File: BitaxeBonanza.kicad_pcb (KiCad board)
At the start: 6 copper layers, 65 x 112 mm, 174 parts, among them J1 XT30, J3 Conn_01x04, J4 USB_C_Receptacle_USB2.0, J5 Conn_01x06, J7 Conn_01x04, J8 TC2030-IDC, SW1 SWITCH-SPST, SW2 SWITCH-SPST, U1 TPS546D24ARVFR, U10 25MHz, U11 Treasure L2R, U12 Treasure R2L, U13 EMC2103-2, U14 SN74AVC4T774, U15 ISO6520, U2 TLV75515PDQNR, U3 TPSM861253RDXR, U4 TPS546D24ARVFR, U5 L78L05_SOT89, U6 ESP32-S3-WROOM-1, U7 TLV755075PDQNR, U8 TLV75515PDQNR, U9 TLV755075PDQNR

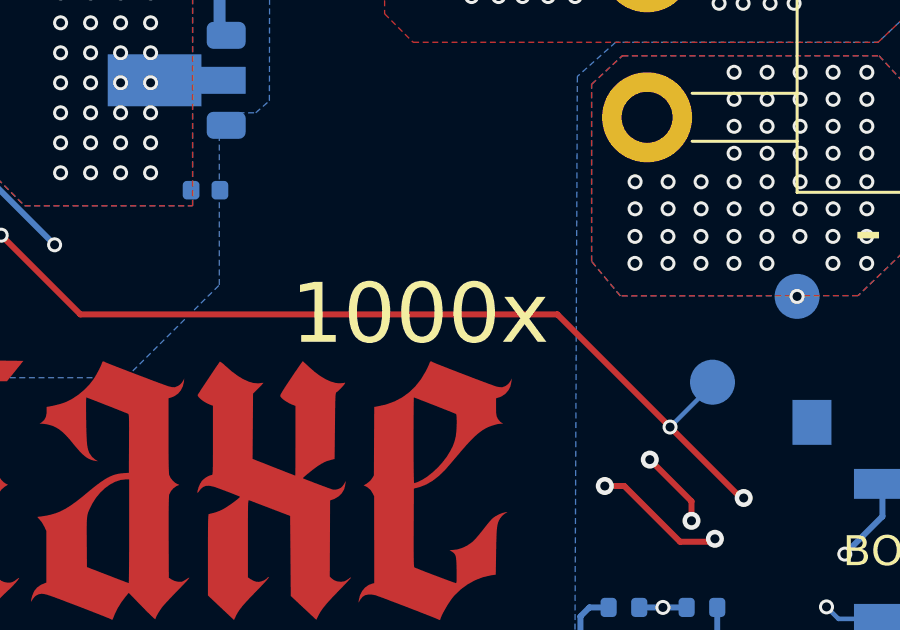
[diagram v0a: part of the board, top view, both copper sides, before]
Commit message: added 8 ASICs in schematic
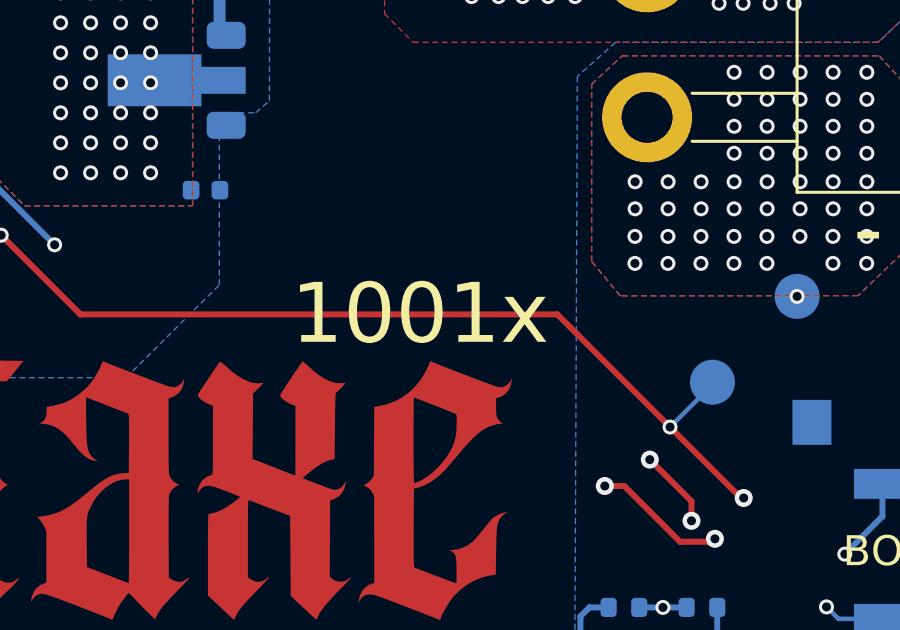
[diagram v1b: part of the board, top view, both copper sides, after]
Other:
- board text added: "1001x"
- board text removed: "1000x"
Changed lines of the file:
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@@
 		)
 	)
-	(gr_text "1000x"
+	(gr_text "1001x"
 		(at 138.48 67.98 0)
 		(layer "F.SilkS")

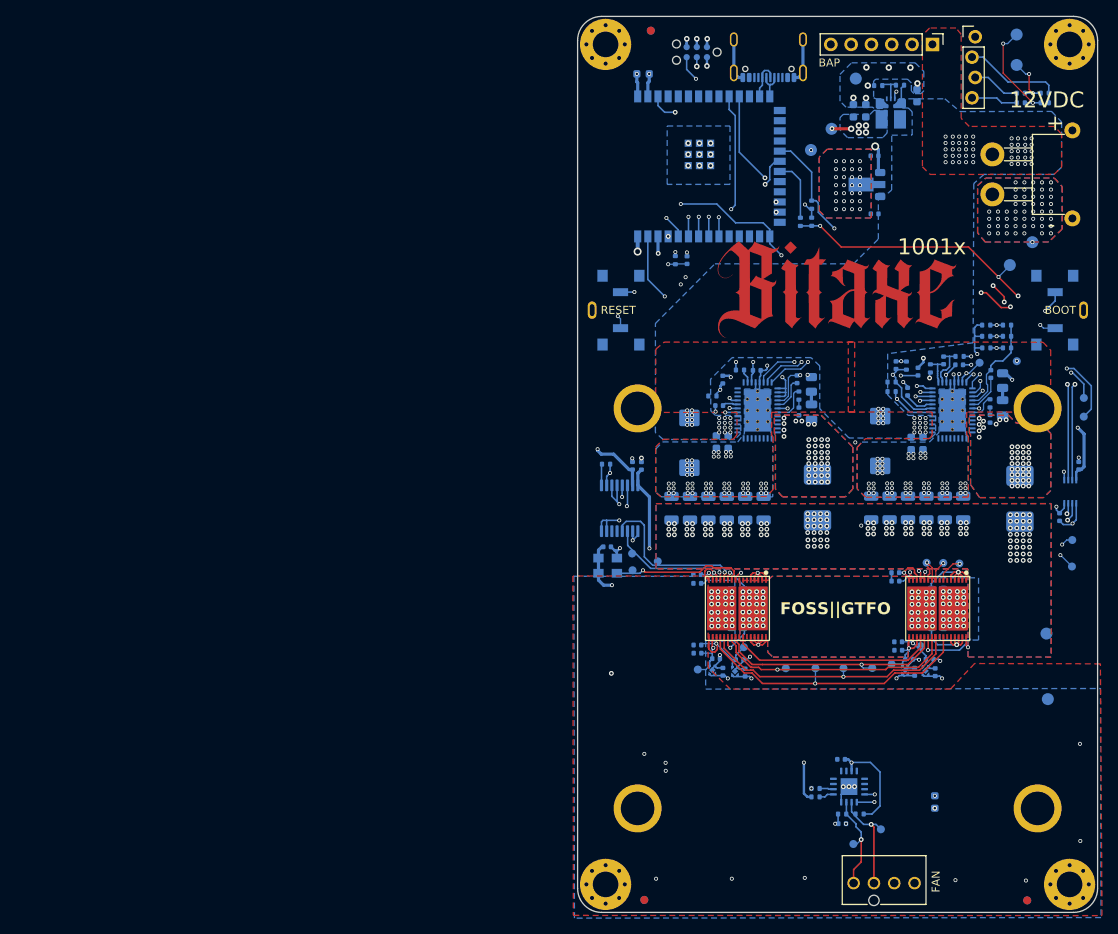
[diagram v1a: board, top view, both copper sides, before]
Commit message: moved ASIC bypass caps out to separate sheet
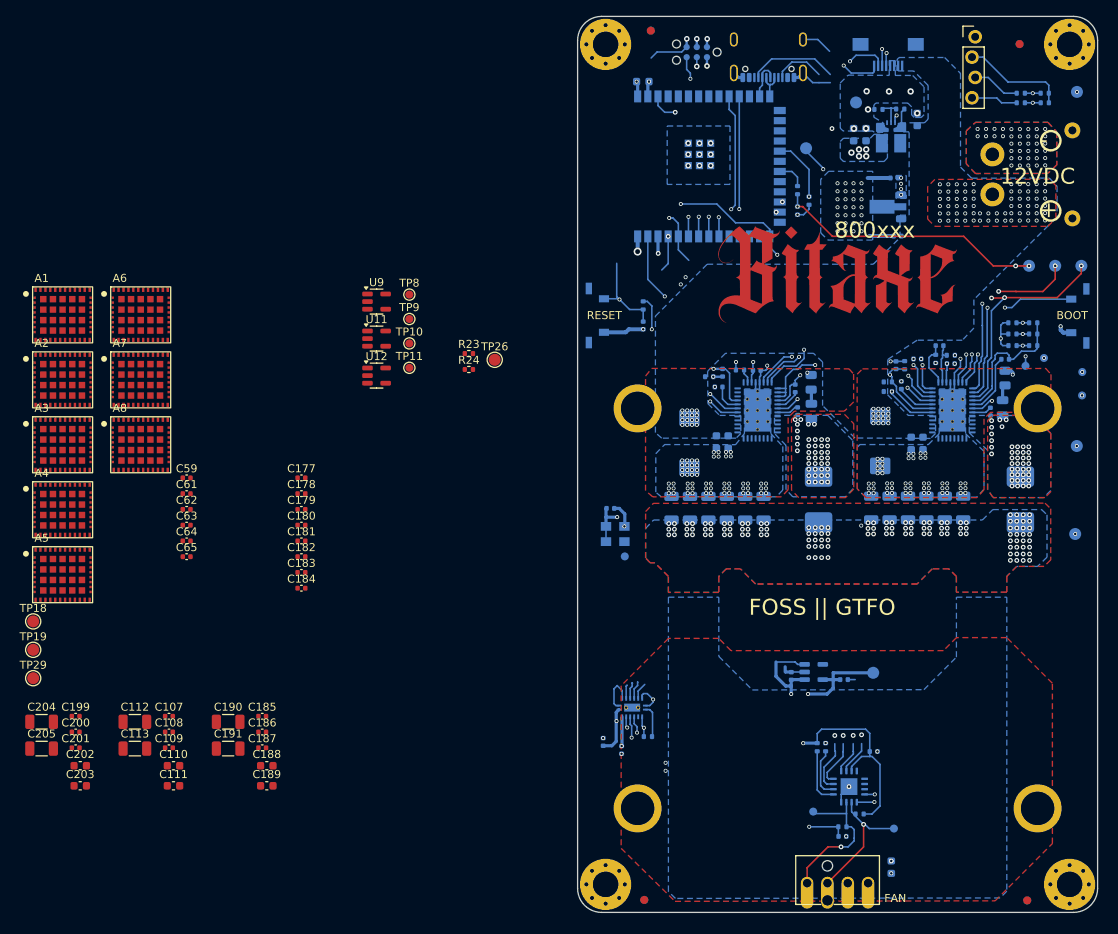
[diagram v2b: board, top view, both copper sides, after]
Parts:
- removed the C21 at (119.4, 120.0)
- removed the C38 at (116.7, 119.9)
- removed C40, C50, C51, C52, C53, C54, C57, C58: 1uF, Capacitor_SMD:C_0402_1005Metric
- removed C66, C67, C68, C69, C73, C74, C75, C76: 10uF, Capacitor_SMD:C_0603_1608Metric
- removed C70, C71: 0.1uF, Capacitor_SMD:C_0402_1005Metric
- removed FID5, FID6: Fiducial_back, Fiducial:Fiducial_1mm_Mask2mm
- removed H16: Heatsink Mounts, bitaxe:GT_heatsink
- removed J5: Conn_01x06, Connector_PinHeader_2.54mm:PinHeader_1x06_P2.54mm_Vertical
- removed TP12, TP13, TP14: ~, TestPoint:TestPoint_Pad_D1.0mm
- removed TP2: 1V5, TestPoint:TestPoint_Pad_D1.0mm
- removed TP4: 0V75, TestPoint:TestPoint_Pad_D1.0mm
- removed TP5: 1V5-0, TestPoint:TestPoint_Pad_D1.0mm
- removed TP6: 0V75-0, TestPoint:TestPoint_Pad_D1.0mm
- removed U14: SN74AVC4T774, Package_SO:TSSOP-16_4.4x5mm_P0.65mm
- removed U15: ISO6520, bitaxe:ISO6520FREUR
- removed U8: TLV75515PDQNR, bitaxe:DQN0004A
- added A1: BZM2_MODE1, bitaxe:bzm2, F.Cu at (34.1, 75.3)
- added A2: BZM2_MODE1, bitaxe:bzm2, F.Cu at (34.1, 83.4)
- added A3: BZM2_MODE0, bitaxe:bzm2, F.Cu at (34.1, 91.5)
- added A4: BZM2_MODE0, bitaxe:bzm2, F.Cu at (34.1, 99.7)
- added A5: BZM2_MODE1, bitaxe:bzm2, F.Cu at (34.1, 107.8)
- added A6: BZM2_MODE1, bitaxe:bzm2, F.Cu at (43.9, 75.3)
- added A7: BZM2_MODE0, bitaxe:bzm2, F.Cu at (43.9, 83.4)
- added A8: BZM2_MODE0, bitaxe:bzm2, F.Cu at (43.9, 91.5)
- added C107: 0.1uF, Capacitor_SMD:C_0402_1005Metric, F.Cu at (47.4, 125.5)
- added C108: 0.1uF, Capacitor_SMD:C_0402_1005Metric, F.Cu at (47.4, 127.5)
- added C109: 0.1uF, Capacitor_SMD:C_0402_1005Metric, F.Cu at (47.4, 129.4)
- added C110: 10uF, Capacitor_SMD:C_0603_1608Metric, F.Cu at (48.0, 131.7)
- added C111: 10uF, Capacitor_SMD:C_0603_1608Metric, F.Cu at (48.0, 134.2)
- added C112: 100uF, Capacitor_SMD:C_1206_3216Metric, F.Cu at (43.2, 126.2)
- added C113: 100uF, Capacitor_SMD:C_1206_3216Metric, F.Cu at (43.2, 129.5)
- added C177: 120pF, Capacitor_SMD:C_0402_1005Metric, F.Cu at (64.0, 95.7)
- added C178: 120pF, Capacitor_SMD:C_0402_1005Metric, F.Cu at (64.0, 97.7)
- added C179: 120pF, Capacitor_SMD:C_0402_1005Metric, F.Cu at (64.0, 99.6)
- added C180: 120pF, Capacitor_SMD:C_0402_1005Metric, F.Cu at (64.0, 101.6)
- added C181: 120pF, Capacitor_SMD:C_0402_1005Metric, F.Cu at (64.0, 103.6)
- added C182: 120pF, Capacitor_SMD:C_0402_1005Metric, F.Cu at (64.0, 105.5)
- added C183: 120pF, Capacitor_SMD:C_0402_1005Metric, F.Cu at (64.0, 107.5)
- added C184: 120pF, Capacitor_SMD:C_0402_1005Metric, F.Cu at (64.0, 109.5)
- added C185: 0.1uF, Capacitor_SMD:C_0402_1005Metric, F.Cu at (59.1, 125.5)
- added C186: 0.1uF, Capacitor_SMD:C_0402_1005Metric, F.Cu at (59.1, 127.5)
- added C187: 0.1uF, Capacitor_SMD:C_0402_1005Metric, F.Cu at (59.1, 129.4)
- added C188: 10uF, Capacitor_SMD:C_0603_1608Metric, F.Cu at (59.6, 131.7)
- added C189: 10uF, Capacitor_SMD:C_0603_1608Metric, F.Cu at (59.6, 134.2)
- added C190: 100uF, Capacitor_SMD:C_1206_3216Metric, F.Cu at (54.8, 126.2)
- added C191: 100uF, Capacitor_SMD:C_1206_3216Metric, F.Cu at (54.8, 129.5)
- added C199: 0.1uF, Capacitor_SMD:C_0402_1005Metric, F.Cu at (35.8, 125.5)
- added C200: 0.1uF, Capacitor_SMD:C_0402_1005Metric, F.Cu at (35.8, 127.5)
- added C201: 0.1uF, Capacitor_SMD:C_0402_1005Metric, F.Cu at (35.8, 129.4)
- added C202: 10uF, Capacitor_SMD:C_0603_1608Metric, F.Cu at (36.3, 131.7)
- added C203: 10uF, Capacitor_SMD:C_0603_1608Metric, F.Cu at (36.3, 134.2)
- added C204: 100uF, Capacitor_SMD:C_1206_3216Metric, F.Cu at (31.5, 126.2)
- added C205: 100uF, Capacitor_SMD:C_1206_3216Metric, F.Cu at (31.5, 129.5)
- added C59: 1uF, Capacitor_SMD:C_0402_1005Metric, F.Cu at (49.6, 95.7)
- added C61: 1uF, Capacitor_SMD:C_0402_1005Metric, F.Cu at (49.6, 97.7)
- added H5: MountingHole_Pad, bitaxe:Sinhoo SMTSO3015CTJ_nopaste, B.Cu at (156.0, 87.0)
- added H6: MountingHole_Pad, bitaxe:Sinhoo SMTSO3015CTJ_nopaste, B.Cu at (106.0, 87.0)
- added H7: MountingHole_Pad, bitaxe:Sinhoo SMTSO3015CTJ_nopaste, B.Cu at (106.0, 137.0)
- added H8: MountingHole_Pad, bitaxe:Sinhoo SMTSO3015CTJ_nopaste, B.Cu at (156.0, 137.0)
- added J2: Conn_01x08, bitaxe:FPC-SMD_P0.50-8P_FGS-XJ-H2.0, B.Cu at (137.3, 42.8)
- C62, C63, C64, C65, R23, R24, TP26: moved to F.Cu
- FID1, FID2, FID3: value Fiducial_front -> Fiducial; footprint Fiducial:Fiducial_1mm_Mask2mm -> bitaxe:Fiducial_1mm_Mask2mm
- FID4: value Fiducial_back -> Fiducial; footprint Fiducial:Fiducial_1mm_Mask2mm -> bitaxe:Fiducial_1mm_Mask2mm; moved to F.Cu
- J1: moved to B.Cu
- SW1, SW2: footprint bitaxe:SW_TL3336AF160Q -> bitaxe:SW_TL3330AF130QG_EWI
- TP10, TP11, TP8, TP9: value ~ -> CLKI; moved to F.Cu
- TP16: value ~ -> 1V2; footprint TestPoint:TestPoint_Pad_D1.0mm -> TestPoint:TestPoint_Pad_D1.5mm
- TP18, TP19, TP29: value ~ -> 1V2; footprint TestPoint:TestPoint_Pad_D1.0mm -> TestPoint:TestPoint_Pad_D1.5mm; moved to F.Cu
- U11: value Treasure L2R -> MCP1824T-1202E/OT; footprint bitaxe:Auradine_Treasure -> Package_TO_SOT_SMD:SOT-23-5
- U12: value Treasure R2L -> MCP1824T-1202E/OT; footprint bitaxe:Auradine_Treasure -> Package_TO_SOT_SMD:SOT-23-5
- U2: value TLV75515PDQNR -> SN74AVC4T774; footprint bitaxe:DQN0004A -> bitaxe:BQB0016A-MFG
- U7: value TLV755075PDQNR -> MCP1824T-1202E/OT; footprint bitaxe:DQN0004A -> Package_TO_SOT_SMD:SOT-23-5
- U9: value TLV755075PDQNR -> MCP1824T-1202E/OT; footprint bitaxe:DQN0004A -> Package_TO_SOT_SMD:SOT-23-5; moved to F.Cu
- moved TP29 104.9 mm to (30.4, 120.7)
- moved TP19 101.3 mm to (30.4, 117.2)
- moved TP18 94.3 mm to (30.4, 113.6)
- moved C63 88.8 mm to (49.6, 101.6)
- moved C65 88.7 mm to (49.6, 105.5)
- moved TP11 86.5 mm to (77.5, 81.9)
- moved U9 82.7 mm to (73.4, 73.7), turned to 0 degrees
- moved TP8 76.5 mm to (77.5, 72.8)
- moved U12 75.9 mm to (73.4, 82.9), turned to 0 degrees
- moved TP9 73.4 mm to (77.5, 75.8)
- moved TP10 70.2 mm to (77.5, 78.9)
- moved R23 65.4 mm to (84.9, 80.1), turned to 0 degrees
- moved C62 64.5 mm to (49.6, 99.6)
- moved C64 64.0 mm to (49.6, 103.6)
- moved U11 56.3 mm to (73.4, 78.3), turned to 0 degrees
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- renumbered C48 to C21, C59 to C38, C61 to C48, R14 to R25
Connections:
- C38 pad 1: /ASIC/1V5 -> /ASIC/1V2
- C38 pad 2: GND -> /ASIC/GND
- C48 pad 2: GND -> /ASIC/GND
- C55 pad 1: GND -> /ASIC/GND
- C55 pad 2: /ASIC/0V75 -> /5V
- C56 pad 1: /ASIC/GND0 -> /ASIC/GND
- C56 pad 2: /ASIC/0V75-0 -> /ASIC/1V2
- C60 pad 2: GND -> /ASIC/GND
- C62 pad 1: GND -> /ASIC/GND2
- C62 pad 2: Net-(C62-Pad2) -> /5V
- C63 pad 1: /ASIC/GND0 -> /ASIC/GND2
- C63 pad 2: Net-(C63-Pad2) -> /ASIC/1V2-2
- C64 pad 1: GND -> /ASIC/GND3
- C64 pad 2: Net-(C64-Pad2) -> /5V
- C65 pad 1: /ASIC/GND0 -> /ASIC/GND3
- C65 pad 2: Net-(C65-Pad2) -> /ASIC/1V2-3
- R25 pad 1: GND -> /ASIC/GND
- R25 pad 2: Net-(U14-OE) -> Net-(U2-OE)
- TP10 pad 1: Net-(U12-CLOCK_O) -> Net-(A8-TX_IN)
- TP11 pad 1: /ASIC/RX_1V5 -> Net-(A8-TRIP_IN)
- TP16 pad 1: Net-(U11-RESET_N_O) -> /ASIC/1V2
- TP18 pad 1: Net-(U11-CLOCK_O) -> /ASIC/1V2-1
- TP19 pad 1: Net-(U11-COMMAND_O) -> /ASIC/1V2-2
- TP29 pad 1: Net-(U11-RESPONSE_O) -> /ASIC/1V2-3
- TP8 pad 1: Net-(U12-RESET_N_O) -> Net-(A8-RX_OUT)
- TP9 pad 1: Net-(U12-COMMAND_O) -> Net-(A8-RESET_OUT)
- U10 pad 2: GND -> /ASIC/GND
- U11 pad 1: GND -> /5V
- U11 pad 2: GND -> /ASIC/GND2
- U11 pad 3: GND -> /5V
- U11 pad 4: GND -> unconnected-(U11-PG-Pad4)
- U11 pad 5: GND -> /ASIC/1V2-2
- U12 pad 1: /ASIC/GND0 -> /5V
- U12 pad 2: /ASIC/GND0 -> /ASIC/GND3
- U12 pad 3: /ASIC/GND0 -> /5V
- U12 pad 4: /ASIC/GND0 -> unconnected-(U12-PG-Pad4)
- U12 pad 5: /ASIC/GND0 -> /ASIC/1V2-3
- U2 pad 1: /ASIC/1V5 -> /ASIC/GND
- U2 pad 2: GND -> /ASIC/GND
- U2 pad 3: /5V -> /ASIC/RST_1V2
- U2 pad 4: /5V -> /ASIC/TX_1V2
- U2 pad 5: GND -> /ASIC/RX_1V2
- U6 pad 20: /ASIC/TT_3V3 -> /ASIC/TRIP_3V3
- U7 pad 1: /ASIC/0V75 -> /5V
- U7 pad 2: GND -> /ASIC/GND
- U7 pad 4: /5V -> unconnected-(U7-PG-Pad4)
- U7 pad 5: GND -> /ASIC/1V2
- U9 pad 1: /ASIC/0V75-0 -> /5V
- U9 pad 2: /ASIC/GND0 -> /ASIC/GND1
- U9 pad 4: /5V -> unconnected-(U9-PG-Pad4)
- U9 pad 5: /ASIC/GND0 -> /ASIC/1V2-1
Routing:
- net (no net): track 0.00 -> 111.2 mm, vias 0 -> 4
- net /ASIC/1V2: track 0.00 -> 80.1 mm, vias 0 -> 4
- net /ASIC/TT_3V3: track 70.7 -> 0.00 mm, vias 2 -> 0
- net /3V3: track 213.7 -> 145.5 mm, vias 16 -> 13
- net /ASIC/GND0: track 65.9 -> 0.00 mm, vias 55 -> 0
- net /ASIC/1V5: track 61.5 -> 0.00 mm, vias 4 -> 0
- net /ASIC/1V5-0: track 44.0 -> 0.00 mm, vias 3 -> 0
- net Net-(U11-RESET_N_O): track 36.7 -> 0.00 mm, vias 1 -> 0
- net Net-(U11-COMMAND_O): track 33.8 -> 0.00 mm, vias 1 -> 0
- net /ASIC/TX_3V3: track 59.7 -> 93.5 mm
- net GND: track 81.8 -> 48.3 mm, vias 262 -> 216
- net Net-(U11-CLOCK_O): track 31.6 -> 0.00 mm, vias 1 -> 0
- net Net-(U11-RESPONSE_O): track 29.8 -> 0.00 mm, vias 1 -> 0
- net /ASIC/RX_1V5: track 29.1 -> 0.00 mm, vias 3 -> 0
- net /ASIC/TT_1V5: track 28.8 -> 0.00 mm, vias 3 -> 0
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- added copper zone on B.Cu, net /5V
- removed copper zone on B.Cu, net /ASIC/GND0
- removed copper zone on F.Cu, net /ASIC/GND0
- removed copper zone on In2.Cu, net /ASIC/GND0
- removed copper zone on In4.Cu, net /Power/SW2
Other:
- board text added: "800xxx"
- board text added: "FOSS || GTFO"
- board text removed: "1001x"
- board text removed: "FOSS||GTFO"

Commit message: made the board double wide. rough ASIC and vreg placement.
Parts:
- removed the TP16 at (135.4, 120.0)
- added C100: 10uF, Capacitor_SMD:C_0603_1608Metric, F.Cu at (38.0, 40.0)
- added C101: 100uF, Capacitor_SMD:C_1206_3216Metric, F.Cu at (33.1, 32.0)
- added C102: 100uF, Capacitor_SMD:C_1206_3216Metric, F.Cu at (33.1, 35.4)
- added C103: 0.1uF, Capacitor_SMD:C_0402_1005Metric, F.Cu at (72.4, 44.3)
- added C104: 0.1uF, Capacitor_SMD:C_0402_1005Metric, F.Cu at (72.4, 46.3)
- added C105: 0.1uF, Capacitor_SMD:C_0402_1005Metric, F.Cu at (72.4, 48.2)
- added C106: 10uF, Capacitor_SMD:C_0603_1608Metric, F.Cu at (73.0, 50.5)
- added C114: 10uF, Capacitor_SMD:C_0603_1608Metric, F.Cu at (61.3, 53.0)
- added C115: 100uF, Capacitor_SMD:C_1206_3216Metric, F.Cu at (56.5, 45.0)
- added C116: 100uF, Capacitor_SMD:C_1206_3216Metric, F.Cu at (56.5, 48.3)
- added C117: 0.1uF, Capacitor_SMD:C_0402_1005Metric, F.Cu at (37.4, 44.3)
- added C118: 0.1uF, Capacitor_SMD:C_0402_1005Metric, F.Cu at (37.4, 46.3)
- added C119: 0.1uF, Capacitor_SMD:C_0402_1005Metric, F.Cu at (37.4, 48.2)
- added C120: 10uF, Capacitor_SMD:C_0603_1608Metric, F.Cu at (38.0, 50.5)
- added C121: 10uF, Capacitor_SMD:C_0603_1608Metric, F.Cu at (38.0, 53.0)
- added C122: 100uF, Capacitor_SMD:C_1206_3216Metric, F.Cu at (33.1, 45.0)
- added C123: 100uF, Capacitor_SMD:C_1206_3216Metric, F.Cu at (33.1, 48.3)
- added C124: 0.1uF, Capacitor_SMD:C_0402_1005Metric, F.Cu at (60.7, 31.4)
- added C125: 0.1uF, Capacitor_SMD:C_0402_1005Metric, F.Cu at (60.7, 33.3)
- added C126: 0.1uF, Capacitor_SMD:C_0402_1005Metric, F.Cu at (60.7, 35.3)
- added C127: 10uF, Capacitor_SMD:C_0603_1608Metric, F.Cu at (61.3, 37.5)
- added C128: 10uF, Capacitor_SMD:C_0603_1608Metric, F.Cu at (61.3, 40.0)
- added C129: 100uF, Capacitor_SMD:C_1206_3216Metric, F.Cu at (56.5, 32.0)
- added C130: 100uF, Capacitor_SMD:C_1206_3216Metric, F.Cu at (56.5, 35.4)
- added C131: 0.1uF, Capacitor_SMD:C_0402_1005Metric, F.Cu at (72.4, 31.4)
- added C132: 0.1uF, Capacitor_SMD:C_0402_1005Metric, F.Cu at (72.4, 33.3)
- added C133: 0.1uF, Capacitor_SMD:C_0402_1005Metric, F.Cu at (72.4, 35.3)
- added C134: 10uF, Capacitor_SMD:C_0603_1608Metric, F.Cu at (73.0, 37.5)
- added C135: 10uF, Capacitor_SMD:C_0603_1608Metric, F.Cu at (73.0, 40.0)
- added C136: 100uF, Capacitor_SMD:C_1206_3216Metric, F.Cu at (68.1, 32.0)
- added C137: 100uF, Capacitor_SMD:C_1206_3216Metric, F.Cu at (68.1, 35.4)
- added C138: 0.1uF, Capacitor_SMD:C_0402_1005Metric, F.Cu at (49.1, 18.4)
- added C139: 0.1uF, Capacitor_SMD:C_0402_1005Metric, F.Cu at (49.1, 20.4)
- added C140: 0.1uF, Capacitor_SMD:C_0402_1005Metric, F.Cu at (49.1, 22.4)
- added C141: 10uF, Capacitor_SMD:C_0603_1608Metric, F.Cu at (49.6, 24.6)
- added C142: 10uF, Capacitor_SMD:C_0603_1608Metric, F.Cu at (49.6, 27.1)
- added C143: 100uF, Capacitor_SMD:C_1206_3216Metric, F.Cu at (44.8, 19.1)
- added C144: 100uF, Capacitor_SMD:C_1206_3216Metric, F.Cu at (44.8, 22.5)
- added C145: 0.1uF, Capacitor_SMD:C_0402_1005Metric, F.Cu at (60.7, 18.4)
- added C146: 0.1uF, Capacitor_SMD:C_0402_1005Metric, F.Cu at (60.7, 20.4)
- added C147: 0.1uF, Capacitor_SMD:C_0402_1005Metric, F.Cu at (60.7, 22.4)
- added C148: 10uF, Capacitor_SMD:C_0603_1608Metric, F.Cu at (61.3, 24.6)
- added C149: 10uF, Capacitor_SMD:C_0603_1608Metric, F.Cu at (61.3, 27.1)
- added C150: 100uF, Capacitor_SMD:C_1206_3216Metric, F.Cu at (56.5, 19.1)
- added C151: 100uF, Capacitor_SMD:C_1206_3216Metric, F.Cu at (56.5, 22.5)
- added C152: 0.1uF, Capacitor_SMD:C_0402_1005Metric, F.Cu at (49.1, 57.2)
- added C153: 0.1uF, Capacitor_SMD:C_0402_1005Metric, F.Cu at (49.1, 59.2)
- added C154: 0.1uF, Capacitor_SMD:C_0402_1005Metric, F.Cu at (49.1, 61.2)
- added C155: 10uF, Capacitor_SMD:C_0603_1608Metric, F.Cu at (49.6, 63.4)
- added C156: 10uF, Capacitor_SMD:C_0603_1608Metric, F.Cu at (49.6, 65.9)
- added C157: 100uF, Capacitor_SMD:C_1206_3216Metric, F.Cu at (44.8, 57.9)
- added C158: 100uF, Capacitor_SMD:C_1206_3216Metric, F.Cu at (44.8, 61.3)
- added C159: 0.1uF, Capacitor_SMD:C_0402_1005Metric, F.Cu at (72.4, 18.4)
- added C160: 0.1uF, Capacitor_SMD:C_0402_1005Metric, F.Cu at (72.4, 20.4)
- added C161: 0.1uF, Capacitor_SMD:C_0402_1005Metric, F.Cu at (72.4, 22.4)
- added C162: 10uF, Capacitor_SMD:C_0603_1608Metric, F.Cu at (73.0, 24.6)
- added C163: 10uF, Capacitor_SMD:C_0603_1608Metric, F.Cu at (73.0, 27.1)
- added C164: 100uF, Capacitor_SMD:C_1206_3216Metric, F.Cu at (68.1, 19.1)
- added C165: 100uF, Capacitor_SMD:C_1206_3216Metric, F.Cu at (68.1, 22.5)
- added C166: 0.1uF, Capacitor_SMD:C_0402_1005Metric, F.Cu at (49.1, 44.3)
- added C167: 0.1uF, Capacitor_SMD:C_0402_1005Metric, F.Cu at (49.1, 46.3)
- added C168: 0.1uF, Capacitor_SMD:C_0402_1005Metric, F.Cu at (49.1, 48.2)
- added C169: 10uF, Capacitor_SMD:C_0603_1608Metric, F.Cu at (49.6, 50.5)
- added C170: 10uF, Capacitor_SMD:C_0603_1608Metric, F.Cu at (49.6, 53.0)
- added C171: 100uF, Capacitor_SMD:C_1206_3216Metric, F.Cu at (44.8, 45.0)
- added C172: 100uF, Capacitor_SMD:C_1206_3216Metric, F.Cu at (44.8, 48.3)
- added C173: 0.1uF, Capacitor_SMD:C_0402_1005Metric, F.Cu at (49.1, 31.4)
- added C174: 0.1uF, Capacitor_SMD:C_0402_1005Metric, F.Cu at (49.1, 33.3)
- added C175: 0.1uF, Capacitor_SMD:C_0402_1005Metric, F.Cu at (49.1, 35.3)
- added C176: 10uF, Capacitor_SMD:C_0603_1608Metric, F.Cu at (49.6, 37.5)
- added C177: 10uF, Capacitor_SMD:C_0603_1608Metric, F.Cu at (49.6, 40.0)
- added C178: 100uF, Capacitor_SMD:C_1206_3216Metric, F.Cu at (44.8, 32.0)
- added C179: 100uF, Capacitor_SMD:C_1206_3216Metric, F.Cu at (44.8, 35.4)
- added C180: 1000pF, Capacitor_SMD:C_0402_1005Metric, B.Cu at (135.9, 119.2)
- added C181: 1000pF, Capacitor_SMD:C_0402_1005Metric, B.Cu at (167.8, 133.2)
- added C182: 1000pF, Capacitor_SMD:C_0402_1005Metric, B.Cu at (244.2, 97.7)
- added C68: 0.1uF, Capacitor_SMD:C_0402_1005Metric, F.Cu at (37.2, 19.0)
- added C69: 0.1uF, Capacitor_SMD:C_0402_1005Metric, F.Cu at (37.2, 21.0)
- added C70: 0.1uF, Capacitor_SMD:C_0402_1005Metric, F.Cu at (37.2, 22.9)
- added C71: 10uF, Capacitor_SMD:C_0603_1608Metric, F.Cu at (37.7, 25.2)
- added C72: 10uF, Capacitor_SMD:C_0603_1608Metric, F.Cu at (37.7, 27.7)
- added C73: 100uF, Capacitor_SMD:C_1206_3216Metric, F.Cu at (32.9, 19.7)
- added C74: 100uF, Capacitor_SMD:C_1206_3216Metric, F.Cu at (32.9, 23.1)
- added C82: 0.1uF, Capacitor_SMD:C_0402_1005Metric, F.Cu at (37.4, 57.2)
- added C83: 0.1uF, Capacitor_SMD:C_0402_1005Metric, F.Cu at (37.4, 59.2)
- added C84: 0.1uF, Capacitor_SMD:C_0402_1005Metric, F.Cu at (37.4, 61.2)
- added C85: 10uF, Capacitor_SMD:C_0603_1608Metric, F.Cu at (38.0, 63.4)
- added C86: 10uF, Capacitor_SMD:C_0603_1608Metric, F.Cu at (38.0, 65.9)
- added C87: 100uF, Capacitor_SMD:C_1206_3216Metric, F.Cu at (33.1, 57.9)
- added C88: 100uF, Capacitor_SMD:C_1206_3216Metric, F.Cu at (33.1, 61.3)
- added C96: 0.1uF, Capacitor_SMD:C_0402_1005Metric, F.Cu at (37.4, 31.4)
- added C97: 0.1uF, Capacitor_SMD:C_0402_1005Metric, F.Cu at (37.4, 33.3)
- added C98: 0.1uF, Capacitor_SMD:C_0402_1005Metric, F.Cu at (37.4, 35.3)
- added C99: 10uF, Capacitor_SMD:C_0603_1608Metric, F.Cu at (38.0, 37.5)
- added D1: 1SS380VMTE-17, bitaxe:SOD-323FLUMD2_ROM, B.Cu at (129.2, 118.5)
- added D10: 1SS380VMTE-17, bitaxe:SOD-323FLUMD2_ROM, B.Cu at (237.5, 93.7)
- added D11: 1SS380VMTE-17, bitaxe:SOD-323FLUMD2_ROM, B.Cu at (237.5, 90.3)
- added D12: 1SS380VMTE-17, bitaxe:SOD-323FLUMD2_ROM, B.Cu at (237.5, 86.9)
- added D2: 1SS380VMTE-17, bitaxe:SOD-323FLUMD2_ROM, B.Cu at (129.2, 115.1)
- added D3: 1SS380VMTE-17, bitaxe:SOD-323FLUMD2_ROM, B.Cu at (129.2, 111.7)
- added D4: 1SS380VMTE-17, bitaxe:SOD-323FLUMD2_ROM, B.Cu at (129.2, 108.3)
- added D5: 1SS380VMTE-17, bitaxe:SOD-323FLUMD2_ROM, B.Cu at (161.0, 132.5)
- added D6: 1SS380VMTE-17, bitaxe:SOD-323FLUMD2_ROM, B.Cu at (161.0, 129.1)
- added D7: 1SS380VMTE-17, bitaxe:SOD-323FLUMD2_ROM, B.Cu at (161.0, 125.7)
- added D8: 1SS380VMTE-17, bitaxe:SOD-323FLUMD2_ROM, B.Cu at (161.0, 122.3)
- added D9: 1SS380VMTE-17, bitaxe:SOD-323FLUMD2_ROM, B.Cu at (237.5, 97.1)
- added H10: MountingHole_Pad, bitaxe:Sinhoo SMTSO3015CTJ_nopaste, B.Cu at (221.0, 87.0)
- added H11: MountingHole_Pad, bitaxe:Sinhoo SMTSO3015CTJ_nopaste, B.Cu at (171.0, 137.0)
- added H12: MountingHole_Pad, bitaxe:Sinhoo SMTSO3015CTJ_nopaste, B.Cu at (221.0, 137.0)
- added H13: MountingHole_Pad, MountingHole:MountingHole_3.2mm_M3_Pad_Via, F.Cu at (163.2, 41.5)
- added H14: MountingHole_Pad, MountingHole:MountingHole_3.2mm_M3_Pad_Via, F.Cu at (163.2, 146.5)
- added H9: MountingHole_Pad, bitaxe:Sinhoo SMTSO3015CTJ_nopaste, B.Cu at (171.0, 87.0)
- added R33: 1k, Resistor_SMD:R_0402_1005Metric, B.Cu at (133.0, 119.2)
- added R34: 1k, Resistor_SMD:R_0402_1005Metric, B.Cu at (133.0, 117.2)
- added R35: 1k, Resistor_SMD:R_0402_1005Metric, B.Cu at (133.0, 115.2)
- added R36: 1k, Resistor_SMD:R_0402_1005Metric, B.Cu at (133.0, 113.2)
- added R37: 1k, Resistor_SMD:R_0402_1005Metric, B.Cu at (133.0, 111.2)
- added R38: 1k, Resistor_SMD:R_0402_1005Metric, B.Cu at (133.0, 109.2)
- added R39: 1k, Resistor_SMD:R_0402_1005Metric, B.Cu at (164.9, 133.2)
- added R40: 1k, Resistor_SMD:R_0402_1005Metric, B.Cu at (164.9, 131.2)
- added R41: 1k, Resistor_SMD:R_0402_1005Metric, B.Cu at (164.9, 129.2)
- added R42: 1k, Resistor_SMD:R_0402_1005Metric, B.Cu at (164.9, 127.2)
- added R43: 1k, Resistor_SMD:R_0402_1005Metric, B.Cu at (164.9, 125.2)
- added R44: 1k, Resistor_SMD:R_0402_1005Metric, B.Cu at (164.9, 123.2)
- added R45: 1k, Resistor_SMD:R_0402_1005Metric, B.Cu at (241.3, 97.7)
- added R46: 1k, Resistor_SMD:R_0402_1005Metric, B.Cu at (241.3, 95.7)
- added R47: 1k, Resistor_SMD:R_0402_1005Metric, B.Cu at (241.3, 93.7)
- added R48: 1k, Resistor_SMD:R_0402_1005Metric, B.Cu at (241.3, 91.8)
- added R49: 1k, Resistor_SMD:R_0402_1005Metric, B.Cu at (241.3, 89.8)
- added R50: 1k, Resistor_SMD:R_0402_1005Metric, B.Cu at (241.3, 87.8)
- added TP22: 1V2, TestPoint:TestPoint_Pad_D1.5mm, F.Cu at (1.27, 1.27)
- C107: value 0.1uF -> 10uF; footprint Capacitor_SMD:C_0402_1005Metric -> Capacitor_SMD:C_0603_1608Metric
- C108, C109: value 0.1uF -> 100uF; footprint Capacitor_SMD:C_0402_1005Metric -> Capacitor_SMD:C_1206_3216Metric
- C110, C111: value 10uF -> 0.1uF; footprint Capacitor_SMD:C_0603_1608Metric -> Capacitor_SMD:C_0402_1005Metric
- C112: value 100uF -> 0.1uF; footprint Capacitor_SMD:C_1206_3216Metric -> Capacitor_SMD:C_0402_1005Metric
- C113: value 100uF -> 10uF; footprint Capacitor_SMD:C_1206_3216Metric -> Capacitor_SMD:C_0603_1608Metric
- C60: renamed from C55; moved to F.Cu
- C64: renamed from C56; moved to F.Cu
- U11: renamed from U7; moved to F.Cu
- moved A8 162.8 mm to (204.4, 119.1), turned to 180 degrees
- moved A7 162.5 mm to (204.4, 108.7), turned to 180 degrees
- moved A5 155.2 mm to (189.0, 119.1), turned to 180 degrees
- moved A6 148.9 mm to (189.0, 108.7), turned to 180 degrees
- moved A4 105.9 mm to (138.2, 119.0), turned to 180 degrees
- moved A3 105.5 mm to (138.2, 108.7), turned to 180 degrees
- moved A1 99.3 mm to (123.3, 119.0), turned to 180 degrees
- moved A2 92.7 mm to (123.3, 108.6), turned to 180 degrees
- moved C111 88.8 mm to (60.7, 46.3)
- moved C110 88.3 mm to (60.7, 44.3)
- moved C108 85.0 mm to (68.1, 45.0)
- moved C109 83.7 mm to (68.1, 48.3)
- moved C113 81.1 mm to (61.3, 50.5)
- moved C112 79.9 mm to (60.7, 48.2)
- moved C107 76.9 mm to (73.0, 53.0)
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- renumbered C39 to C1, C23 to C10, C3 to C11, C24 to C12, C37 to C13, C15 to C16, C16 to C17, C36 to C18, C46 to C2, C19 to C23, C42 to C24, C8 to C25, C29 to C26, C7 to C27, C45 to C29, C47 to C3, C18 to C30, C20 to C31, C9 to C32, C30 to C33, C10 to C34, C31 to C35, C11 to C36, C32 to C37, C12 to C38, C33 to C39, C43 to C4, C13 to C40, C34 to C41, C14 to C42, C35 to C43, C21 to C44, C49 to C45, C60 to C46, C38 to C47, C183 to C49, C44 to C5, C179 to C50, C184 to C51, C180 to C52, C181 to C53, C182 to C54, C177 to C55, C178 to C56, C64 to C57, C62 to C58, C17 to C6, C65 to C61, C63 to C62, C61 to C63, C92 to C65, C41 to C66, C94 to C67, C1 to C7, C185 to C75, C186 to C76, C187 to C77, C188 to C78, C189 to C79, C22 to C8, C190 to C80, C191 to C81, C199 to C89, C2 to C9, C200 to C90, C201 to C91, C202 to C92, C203 to C93, C204 to C94, C205 to C95, J8 to J2, J2 to J4, J4 to J5, J7 to J6, R17 to R1, R5 to R10, R7 to R11, R9 to R12, R10 to R13, R11 to R14, R6 to R15, R12 to R16, R13 to R17, R3 to R18, R16 to R19, R37 to R2, R23 to R20, R2 to R21, R24 to R22, R15 to R23, R19 to R24, R1 to R25, R8 to R26, R20 to R27, R25 to R28, R33 to R29, R38 to R3, R35 to R30, R30 to R32, R39 to R4, R18 to R5, R21 to R6, R40 to R7, R22 to R8, R4 to R9, TP27 to TP1, TP30 to TP10, TP31 to TP11, TP15 to TP12, TP17 to TP13, TP7 to TP14, TP8 to TP15, TP9 to TP16, TP10 to TP17, TP11 to TP18, TP29 to TP19, TP22 to TP2, TP19 to TP20, TP18 to TP21, TP21 to TP23, TP20 to TP24, TP23 to TP3, TP24 to TP4, TP25 to TP5, TP26 to TP6, TP28 to TP7, TP1 to TP8, TP3 to TP9, U3 to U1, U9 to U10, U13 to U12, U5 to U2, U1 to U3, U6 to U5, U10 to U6, U2 to U7, U12 to U8, U11 to U9
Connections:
- A1 pad 1: /ASIC/bypass1-1/in -> /ASIC/bypass1-1/out
- A1 pad 14: /ASIC/GND -> GND
- A1 pad 21: /ASIC/GND -> GND
- A1 pad 22: /ASIC/GND -> GND
- A1 pad 23: /ASIC/GND -> GND
- A1 pad 24: /ASIC/GND -> GND
- A1 pad 25: /ASIC/GND -> GND
- A1 pad 26: /ASIC/GND -> GND
- A1 pad 27: /ASIC/GND -> GND
- A1 pad 28: /ASIC/GND -> GND
- A1 pad 35: /ASIC/GND -> GND
- A1 pad 38: /ASIC/REFCLK1 -> /ASIC/REFCLKOUT1
- A1 pad 43: /ASIC/GND -> GND
- A1 pad 44: /ASIC/GND -> GND
- A1 pad 45: /ASIC/GND -> GND
- A1 pad 46: /ASIC/GND -> GND
- A1 pad 47: /ASIC/GND -> GND
- A1 pad 48: /ASIC/GND -> GND
- A1 pad 53: /ASIC/GND -> GND
- A1 pad 54: /ASIC/GND -> GND
- A1 pad 55: /ASIC/GND -> GND
- A1 pad 56: /ASIC/GND -> GND
- A1 pad 57: /ASIC/GND -> GND
- A1 pad 58: /ASIC/GND -> GND
- A2 pad 1: unconnected-(A2-VDD_INT_1-Pad1) -> /ASIC/bypass2-1/out
- A2 pad 12: unconnected-(A2-VDD_INT_2-Pad12) -> /ASIC/bypass2-2/in
- A2 pad 14: /ASIC/GND -> GND
- A2 pad 15: unconnected-(A2-RX_OUT-Pad15) -> /ASIC/shifter2-3/RX_OUT
- A2 pad 16: unconnected-(A2-RESET_OUT-Pad16) -> /ASIC/shifter2-3/RESET_OUT
- A2 pad 17: unconnected-(A2-TX_IN-Pad17) -> /ASIC/shifter2-3/TX_IN
- A2 pad 18: unconnected-(A2-TRIP_IN-Pad18) -> /ASIC/shifter2-3/TRIP_IN
- A2 pad 21: /ASIC/GND -> GND
- A2 pad 22: /ASIC/GND -> GND
- A2 pad 23: /ASIC/GND -> GND
- A2 pad 24: /ASIC/GND -> GND
- A2 pad 25: /ASIC/GND -> GND
- A2 pad 26: /ASIC/GND -> GND
- A2 pad 27: /ASIC/GND -> GND
- A2 pad 28: /ASIC/GND -> GND
- A2 pad 35: /ASIC/GND -> GND
- A2 pad 43: /ASIC/GND -> GND
- A2 pad 44: /ASIC/GND -> GND
- A2 pad 45: /ASIC/GND -> GND
- A2 pad 46: /ASIC/GND -> GND
- A2 pad 47: /ASIC/GND -> GND
- A2 pad 48: /ASIC/GND -> GND
- A2 pad 53: /ASIC/GND -> GND
- A2 pad 54: /ASIC/GND -> GND
- A2 pad 55: /ASIC/GND -> GND
- A2 pad 56: /ASIC/GND -> GND
- A2 pad 57: /ASIC/GND -> GND
- A2 pad 58: /ASIC/GND -> GND
- A3 pad 1: unconnected-(A3-VDD_INT_1-Pad1) -> /ASIC/bypass3-1/out
- A3 pad 12: unconnected-(A3-VDD_INT_2-Pad12) -> /ASIC/bypass3-2/in
- A3 pad 15: unconnected-(A3-TRIP_OUT-Pad15) -> /ASIC/shifter2-3/TRIP_OUT
- A3 pad 16: unconnected-(A3-TX_OUT-Pad16) -> /ASIC/shifter2-3/TX_OUT
- A3 pad 17: unconnected-(A3-RESET_IN-Pad17) -> /ASIC/shifter2-3/RESET_IN
- A3 pad 18: unconnected-(A3-RX_IN-Pad18) -> /ASIC/shifter2-3/RX_IN
- A3 pad 29: /ASIC/REFCLK1 -> /ASIC/REFCLKIN1
- A3 pad 38: /ASIC/REFCLK2 -> /ASIC/REFCLKOUT2
- A4 pad 1: unconnected-(A4-VDD_INT_1-Pad1) -> /ASIC/bypass4-1/out
- A4 pad 12: unconnected-(A4-VDD_INT_2-Pad12) -> /ASIC/bypass4-2/in
- A4 pad 31: unconnected-(A4-RX_OUT-Pad31) -> /ASIC/shifter4-5/RX_OUT
- A4 pad 32: unconnected-(A4-RESET_OUT-Pad32) -> /ASIC/shifter4-5/RESET_OUT
- A4 pad 33: unconnected-(A4-TX_IN-Pad33) -> /ASIC/shifter4-5/TX_IN
- A4 pad 34: unconnected-(A4-TRIP_IN-Pad34) -> /ASIC/shifter4-5/TRIP_IN
- A5 pad 1: unconnected-(A5-VDD_INT_1-Pad1) -> /ASIC/bypass5-1/out
- A5 pad 12: unconnected-(A5-VDD_INT_2-Pad12) -> /ASIC/bypass5-2/in
- A5 pad 29: /ASIC/REFCLK2 -> /ASIC/REFCLKIN2
- A5 pad 31: unconnected-(A5-TRIP_OUT-Pad31) -> /ASIC/shifter4-5/TRIP_OUT
- A5 pad 32: unconnected-(A5-TX_OUT-Pad32) -> /ASIC/shifter4-5/TX_OUT
- A5 pad 33: unconnected-(A5-RESET_IN-Pad33) -> /ASIC/shifter4-5/RESET_IN
- A5 pad 34: unconnected-(A5-RX_IN-Pad34) -> /ASIC/shifter4-5/RX_IN
- A5 pad 38: /ASIC/REFCLK3 -> /ASIC/REFCLKOUT3
- A6 pad 1: unconnected-(A6-VDD_INT_1-Pad1) -> /ASIC/bypass6-1/out
- A6 pad 12: unconnected-(A6-VDD_INT_2-Pad12) -> /ASIC/bypass6-2/in
- A6 pad 15: unconnected-(A6-RX_OUT-Pad15) -> /ASIC/shifter6-7/RX_OUT
- A6 pad 16: unconnected-(A6-RESET_OUT-Pad16) -> /ASIC/shifter6-7/RESET_OUT
- A6 pad 17: unconnected-(A6-TX_IN-Pad17) -> /ASIC/shifter6-7/TX_IN
- A6 pad 18: unconnected-(A6-TRIP_IN-Pad18) -> /ASIC/shifter6-7/TRIP_IN
- A7 pad 1: /ASIC/bypass/in -> /ASIC/bypass7-1/out
- A7 pad 12: unconnected-(A7-VDD_INT_2-Pad12) -> /ASIC/bypass7-2/in
- A7 pad 15: unconnected-(A7-TRIP_OUT-Pad15) -> /ASIC/shifter6-7/TRIP_OUT
- A7 pad 16: unconnected-(A7-TX_OUT-Pad16) -> /ASIC/shifter6-7/TX_OUT
- A7 pad 17: unconnected-(A7-RESET_IN-Pad17) -> /ASIC/shifter6-7/RESET_IN
- A7 pad 18: unconnected-(A7-RX_IN-Pad18) -> /ASIC/shifter6-7/RX_IN
- A7 pad 29: /ASIC/REFCLK3 -> /ASIC/REFCLKIN3
- A8 pad 1: unconnected-(A8-VDD_INT_1-Pad1) -> /ASIC/bypass8-1/out
- A8 pad 12: unconnected-(A8-VDD_INT_2-Pad12) -> /ASIC/bypass8-2/in
- C107 pad 1: /ASIC/bypass/in -> /ASIC/GND2
- C107 pad 2: /ASIC/GND3 -> /ASIC/bypass4-1/out
- C108 pad 1: /ASIC/bypass/in -> /ASIC/bypass4-1/out
- C108 pad 2: /ASIC/GND3 -> /ASIC/GND2
- C109 pad 1: /ASIC/bypass/in -> /ASIC/bypass4-1/out
- C109 pad 2: /ASIC/GND3 -> /ASIC/GND2
- C110 pad 1: /ASIC/bypass/in -> /ASIC/bypass4-2/in
- C110 pad 2: /ASIC/GND3 -> /ASIC/GND1
- C111 pad 1: /ASIC/bypass/in -> /ASIC/bypass4-2/in
- C111 pad 2: /ASIC/GND3 -> /ASIC/GND1
- C112 pad 1: /ASIC/GND3 -> /ASIC/bypass4-2/in
- C112 pad 2: /ASIC/bypass/in -> /ASIC/GND1
- C113 pad 1: /ASIC/GND3 -> /ASIC/bypass4-2/in
- C113 pad 2: /ASIC/bypass/in -> /ASIC/GND1
- C46 pad 2: /ASIC/GND -> GND
- C47 pad 2: /ASIC/GND -> GND
- C48 pad 2: /ASIC/GND -> GND
- C49 pad 2: Net-(C183-Pad2) -> /ASIC/GND3
- C50 pad 2: Net-(C179-Pad2) -> /ASIC/GND1
- C51 pad 2: Net-(C183-Pad2) -> /ASIC/GND3
- C52 pad 2: Net-(C179-Pad2) -> /ASIC/GND1
- C53 pad 2: Net-(C181-Pad2) -> /ASIC/GND2
- C54 pad 2: Net-(C181-Pad2) -> /ASIC/GND2
- C55 pad 2: Net-(C177-Pad2) -> GND
- C56 pad 2: Net-(C177-Pad2) -> GND
- C60 pad 1: /ASIC/GND -> GND
- C64 pad 1: /ASIC/GND -> GND
- C75 pad 1: /ASIC/bypass1-1/in -> /ASIC/GND1
- C75 pad 2: /ASIC/GND -> /ASIC/bypass1-1/out
- C76 pad 1: /ASIC/bypass1-1/in -> /ASIC/GND1
- C76 pad 2: /ASIC/GND -> /ASIC/bypass1-1/out
- C77 pad 1: /ASIC/bypass1-1/in -> /ASIC/GND1
- C77 pad 2: /ASIC/GND -> /ASIC/bypass1-1/out
- C78 pad 1: /ASIC/bypass1-1/in -> /ASIC/GND1
- C78 pad 2: /ASIC/GND -> /ASIC/bypass1-1/out
- C79 pad 1: /ASIC/bypass1-1/in -> /ASIC/GND1
- C79 pad 2: /ASIC/GND -> /ASIC/bypass1-1/out
- C80 pad 1: /ASIC/GND -> /ASIC/bypass1-1/out
- C80 pad 2: /ASIC/bypass1-1/in -> /ASIC/GND1
- C81 pad 1: /ASIC/GND -> /ASIC/bypass1-1/out
- C81 pad 2: /ASIC/bypass1-1/in -> /ASIC/GND1
- C89 pad 2: /ASIC/GND -> GND
- C90 pad 2: /ASIC/GND -> GND
- C91 pad 2: /ASIC/GND -> GND
- C92 pad 2: /ASIC/GND -> GND
- C93 pad 2: /ASIC/GND -> GND
- C94 pad 1: /ASIC/GND -> GND
- C95 pad 1: /ASIC/GND -> GND
- R28 pad 1: /ASIC/GND -> GND
- U11 pad 2: /ASIC/GND -> GND
- U6 pad 2: /ASIC/GND -> GND
- U7 pad 1: /ASIC/GND -> GND
- U7 pad 10: /ASIC/GND -> GND
- U7 pad 2: /ASIC/GND -> GND
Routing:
- net (no net): track 111.2 -> 2.49 mm, vias 4 -> 1
- net /Power/BP1v5_2: track 15.4 -> 61.0 mm
- net /Power/BCX_DAT: track 49.0 -> 71.9 mm
- net Net-(U3-MSEL1): track 26.1 -> 5.59 mm
- net Net-(U3-VSEL): track 25.8 -> 6.18 mm
- net /Power/SYNC: track 49.5 -> 32.4 mm
- net /Power/BCX_CLK: track 42.7 -> 26.6 mm
- net /ASIC/1V2: track 80.1 -> 67.6 mm, vias 4 -> 3
- net /5V: track 172.4 -> 161.0 mm, vias 7 -> 6
- net /Power/AGND2: track 30.9 -> 41.1 mm
- net /ASIC/GND: track 8.92 -> 0.00 mm
- net Net-(U3-AVIN): track 11.9 -> 6.37 mm
- net GND: track 48.3 -> 53.3 mm, vias 216 -> 217
- net Net-(U3-BOOT): track 2.49 -> 0.00 mm
- net /fan/FAN_TACH: vias 1 -> 2
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- added copper zone on F.Cu, net /ASIC/GND1
- added copper zone on F.Cu, net /ASIC/GND2
- added copper zone on F.Cu, net /ASIC/GND3
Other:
- board size 65 x 112 mm -> 130 x 112 mm
- board text added: "1001x"
- board text removed: "800xxx"

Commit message: switch to EMC2302 for 2 fans and no temp sensor
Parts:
- removed C65, C67: 0.1uF, Capacitor_SMD:C_0402_1005Metric
- removed C66: 10uF, Capacitor_SMD:C_0603_1608Metric
- removed J6: Conn_01x04, bitaxe:470531000
- removed R29: Rshdn, Resistor_SMD:R_0402_1005Metric
- removed R30: Rtrip, Resistor_SMD:R_0402_1005Metric
- removed R31: 5.6k, Resistor_SMD:R_0402_1005Metric
- removed R32: 10k, Resistor_SMD:R_0402_1005Metric
- removed TP23, TP24: TestPoint, TestPoint:TestPoint_Pad_D1.0mm
- removed U12: EMC2103-2, Package_DFN_QFN:QFN-16-1EP_4x4mm_P0.65mm_EP2.1x2.1mm
- added C183: 311-3342-1-ND, Capacitor_SMD:C_0402_1005Metric, F.Cu at (154.2, 177.7)
- added C184: 220uF, Capacitor_SMD:CP_Elec_6.3x7.7, F.Cu at (140.1, 165.5)
- added C185: 220uF, Capacitor_SMD:CP_Elec_6.3x7.7, F.Cu at (140.1, 173.6)
- added C186: 311-3342-1-ND, Capacitor_SMD:C_0402_1005Metric, F.Cu at (154.2, 179.7)
- added C187: 311-3342-1-ND, Capacitor_SMD:C_0402_1005Metric, F.Cu at (154.2, 181.6)
- added J7: Conn_01x04, bitaxe:470531000, F.Cu at (147.4, 165.0)
- added J8: Conn_01x04, bitaxe:470531000, F.Cu at (147.4, 172.7)
- added R51: 5.6k, Resistor_SMD:R_0402_1005Metric, F.Cu at (157.1, 177.7)
- added R52: 5.6k, Resistor_SMD:R_0402_1005Metric, F.Cu at (157.1, 179.7)
- added TP25: TestPoint, TestPoint:TestPoint_Pad_D1.0mm, F.Cu at (158.6, 162.9)
- added TP26: TestPoint, TestPoint:TestPoint_Pad_D1.0mm, F.Cu at (158.6, 166.0)
- added TP27: TestPoint, TestPoint:TestPoint_Pad_D1.0mm, F.Cu at (158.6, 169.0)
- added TP28: TestPoint, TestPoint:TestPoint_Pad_D1.0mm, F.Cu at (158.6, 172.1)
- added U13: EMC2302, Package_SO:MSOP-10_3x3mm_P0.5mm, F.Cu at (145.2, 184.5)
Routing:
- net /3V3: track 145.5 -> 119.9 mm, vias 13 -> 12
- net /fan/FAN_PWM: track 19.0 -> 0.00 mm, vias 3 -> 0
- net /fan/FAN_TACH: track 16.8 -> 0.00 mm, vias 2 -> 0
- net Net-(U12-SHDN_SEL): track 7.09 -> 0.00 mm
- net unconnected-(U12-DN2-Pad15): track 6.63 -> 0.00 mm
- net Net-(U12-TRIP_SET): track 6.33 -> 0.00 mm
- net unconnected-(U12-DP2-Pad16): track 5.89 -> 0.00 mm
- net /5V: track 161.0 -> 156.2 mm, vias 6 -> 5
- net unconnected-(U12-DP1-Pad2): track 4.21 -> 0.00 mm
- net unconnected-(U12-DN1-Pad1): track 4.06 -> 0.00 mm
- net GND: track 53.3 -> 51.0 mm, vias 217 -> 211
- net /ESP32/SCL: track 163.7 -> 161.5 mm, vias 4 -> 3
- net /ESP32/SDA: track 162.3 -> 161.0 mm
- net /12V: vias 101 -> 100
- net (no net): vias 1 -> 0
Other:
- board text removed: "FAN"
